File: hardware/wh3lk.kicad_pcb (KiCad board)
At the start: 4 copper layers, 45 x 33.5 mm, 23 parts, among them J1 Eurorack_Power, J2 Conn_01x08_Pin, U1 LD1117S33TR_SOT223, U2 LM4040DBZ-10

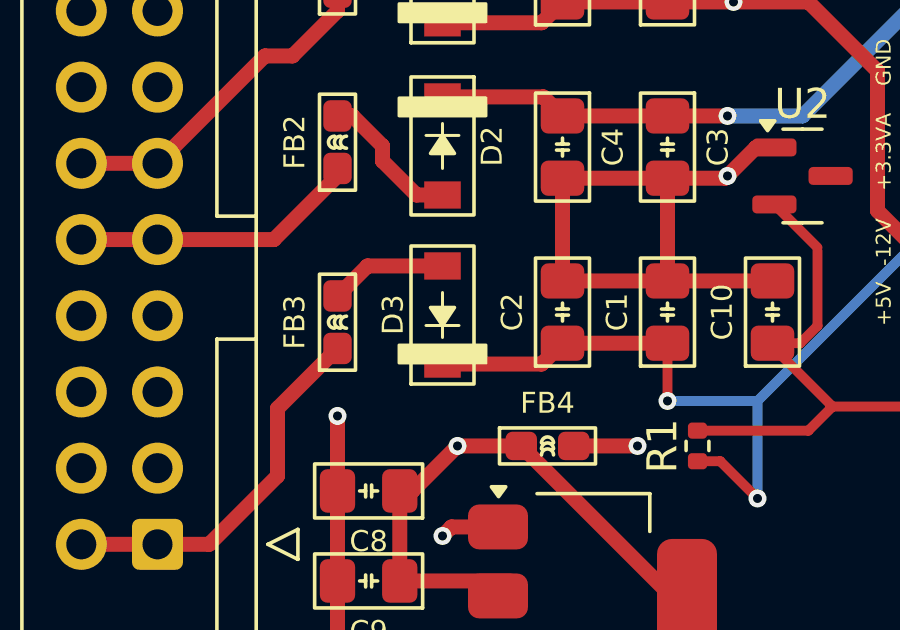
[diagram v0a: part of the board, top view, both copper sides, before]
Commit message: Flipped -12V rail b/c I had it wrong
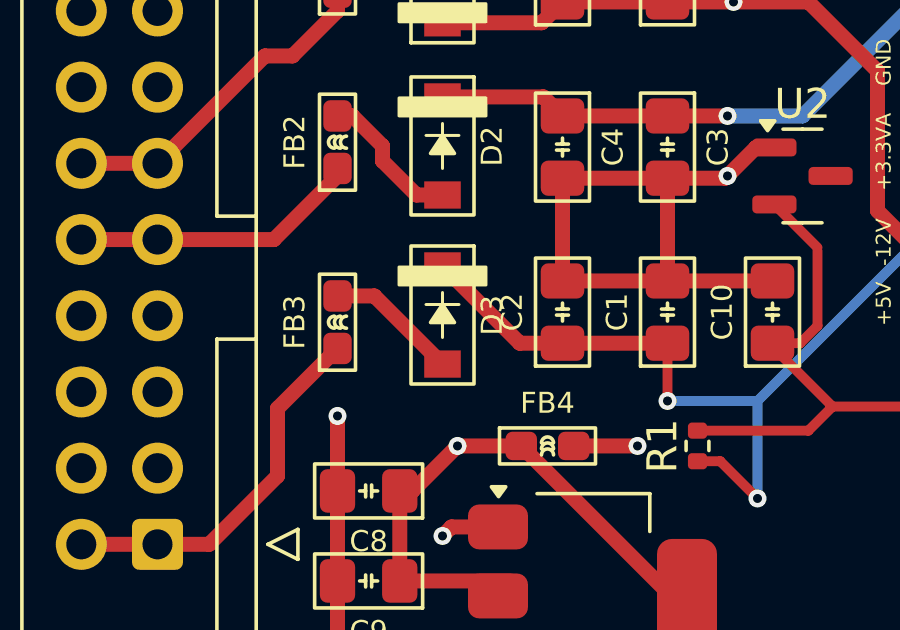
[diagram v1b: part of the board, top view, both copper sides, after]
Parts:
- turned D3 to -90 degrees
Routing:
- net -12V: track 27.9 -> 28.7 mm
- net Net-(D3-A): track 3.91 -> 4.44 mm
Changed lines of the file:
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@@
 	(footprint "winterbloom:D_SOD-123"
 		(layer "F.Cu")
-		(at 73.5 76.635 90)
+		(at 73.5 76.635 -90)
 		(descr "SOD-123")
 		(tags "SOD-123")
 		(property "Reference" "D3"
-			(at 0.01 -1.65 -90)
+			(at 0.01 -1.65 90)
 			(layer "F.SilkS")
 			(effects
@@
 		)
 		(property "Value" "30V"
-			(at 0 2.1 -90)
+			(at 0 2.1 90)
 			(layer "F.Fab")
 			(effects
@@
 		)
 		(property "Footprint" "winterbloom:D_SOD-123"
-			(at 0 0 90)
+			(at 0 0 -90)
 			(unlocked yes)
 			(layer "F.Fab")
@@
 		)
 		(property "Datasheet" ""
-			(at 0 0 90)
+			(at 0 0 -90)
 			(unlocked yes)
 			(layer "F.Fab")
@@
 		)
 		(property "Description" "Diode"
-			(at 0 0 90)
+			(at 0 0 -90)
 			(unlocked yes)
 			(layer "F.Fab")
@@
 		)
 		(property "Sim.Device" "D"
-			(at 0 0 90)
+			(at 0 0 -90)
 			(unlocked yes)
 			(layer "F.Fab")
@@
 		)
 		(property "Sim.Pins" "1=K 2=A"
-			(at 0 0 90)
+			(at 0 0 -90)
 			(unlocked yes)
 			(layer "F.Fab")
@@
 		)
 		(property "LCSC" "C552852"
-			(at 0 0 90)
+			(at 0 0 -90)
 			(unlocked yes)
 			(layer "F.Fab")
@@
 		(attr smd)
 		(fp_line
-			(start 0.25 0)
-			(end 0.75 0)
+			(start -0.75 0)
+			(end -0.35 0)
 			(stroke
 				(width 0.1)
@@
 		(fp_line
 			(start -0.35 0)
-			(end -0.35 -0.55)
+			(end -0.35 0.55)
 			(stroke
 				(width 0.1)
@@
 		(fp_line
 			(start -0.35 0)
-			(end -0.35 0.55)
+			(end -0.35 -0.55)
 			(stroke
 				(width 0.1)
@@
 		)
 		(fp_line
-			(start -0.75 0)
-			(end -0.35 0)
+			(start 0.25 0)
+			(end 0.75 0)
 			(stroke
 				(width 0.1)
@@
 		)
 		(fp_line
-			(start 2 -0.6)
-			(end 2 0.6)
+			(start -0.8 0.6)
+			(end -2 0.6)
 			(stroke
 				(width 0.05)
@@
 		)
 		(fp_line
-			(start 0.8 -0.6)
-			(end 2 -0.6)
+			(start -0.8 0.6)
+			(end -0.8 -0.6)
 			(stroke
 				(width 0.05)
@@
 		)
 		(fp_line
-			(start -0.8 -0.6)
-			(end -2 -0.6)
+			(start 0.8 0.6)
+			(end 2 0.6)
 			(stroke
 				(width 0.05)
@@
 		)
 		(fp_line
-			(start -2 -0.6)
-			(end -2 0.6)
+			(start 0.8 0.6)
+			(end 0.8 -0.6)
 			(stroke
 				(width 0.05)
@@
 		)
 		(fp_line
-			(start 0.8 0.6)
-			(end 0.8 -0.6)
+			(start -2 -0.6)
+			(end -2 0.6)
 			(stroke
 				(width 0.05)
@@
 		)
 		(fp_line
-			(start 0.8 0.6)
-			(end 2 0.6)
+			(start -0.8 -0.6)
+			(end -2 -0.6)
 			(stroke
 				(width 0.05)
@@
 		)
 		(fp_line
-			(start -0.8 0.6)
-			(end -0.8 -0.6)
+			(start 0.8 -0.6)
+			(end 2 -0.6)
 			(stroke
 				(width 0.05)
@@
 		)
 		(fp_line
-			(start -0.8 0.6)
-			(end -2 0.6)
+			(start 2 -0.6)
+			(end 2 0.6)
 			(stroke
 				(width 0.05)
@@
 		)
 		(fp_line
-			(start 2.4 -1.15)
-			(end 2.4 1.15)
+			(start 2.4 1.15)
+			(end -2.4 1.15)
 			(stroke
 				(width 0.05)
@@
 		(fp_line
 			(start -2.4 -1.15)
-			(end 2.4 -1.15)
+			(end -2.4 1.15)
 			(stroke
 				(width 0.05)
@@
 		(fp_line
 			(start -2.4 -1.15)
-			(end -2.4 1.15)
+			(end 2.4 -1.15)
 			(stroke
 				(width 0.05)
@@
 		)
 		(fp_line
-			(start 2.4 1.15)
-			(end -2.4 1.15)
+			(start 2.4 -1.15)
+			(end 2.4 1.15)
 			(stroke
 				(width 0.05)
@@
 		)
 		(fp_line
-			(start 1.6 -1.05)
-			(end 1.6 1.05)
+			(start -1.6 1.05)
+			(end -1.6 -1.05)
 			(stroke
 				(width 0.1)
@@
 		)
 		(fp_line
-			(start -1.6 -1.05)
-			(end 1.6 -1.05)
+			(start 1.6 1.05)
+			(end -1.6 1.05)
 			(stroke
 				(width 0.1)
@@
 		)
 		(fp_line
-			(start 2.3 -0.81)
-			(end 2.3 0.81)
+			(start -1.6 0.81)
+			(end -2.3 0.81)
 			(stroke
 				(width 0.1)
@@
 		)
 		(fp_line
-			(start 1.6 -0.81)
-			(end 2.3 -0.81)
+			(start 1.6 0.81)
+			(end 2.3 0.81)
 			(stroke
 				(width 0.1)
@@
 		)
 		(fp_line
-			(start -1.6 -0.81)
-			(end -2.3 -0.81)
+			(start -2.3 -0.81)
+			(end -2.3 0.81)
 			(stroke
 				(width 0.1)
@@
 		)
 		(fp_line
-			(start -2.3 -0.81)
-			(end -2.3 0.81)
+			(start -1.6 -0.81)
+			(end -2.3 -0.81)
 			(stroke
 				(width 0.1)
@@
 		)
 		(fp_line
-			(start 1.6 0.81)
-			(end 2.3 0.81)
+			(start 1.6 -0.81)
+			(end 2.3 -0.81)
 			(stroke
 				(width 0.1)
@@
 		)
 		(fp_line
-			(start -1.6 0.81)
-			(end -2.3 0.81)
+			(start 2.3 -0.81)
+			(end 2.3 0.81)
 			(stroke
 				(width 0.1)
@@
 		)
 		(fp_line
-			(start 1.6 1.05)
-			(end -1.6 1.05)
+			(start -1.6 -1.05)
+			(end 1.6 -1.05)
 			(stroke
 				(width 0.1)
@@
 		)
 		(fp_line
-			(start -1.6 1.05)
-			(end -1.6 -1.05)
+			(start 1.6 -1.05)
+			(end 1.6 1.05)
 			(stroke
 				(width 0.1)
@@
 		)
 		(fp_text user "${REFERENCE}"
-			(at 0 0 -90)
+			(at 0 0 90)
 			(layer "F.Fab")
 			(effects
@@
 		)
 		(pad "1" smd rect
-			(at -1.635 0 90)
+			(at -1.635 0 270)
 			(size 0.91 1.22)
 			(layers "F.Cu" "F.Paste" "F.Mask")
@@
 		)
 		(pad "2" smd rect
-			(at 1.635 0 90)
+			(at 1.635 0 270)
 			(size 0.91 1.22)
 			(layers "F.Cu" "F.Paste" "F.Mask")
@@
 	)
 	(segment
-		(start 73.5 78.27)
-		(end 76.805 78.27)
+		(start 76.075 77.575)
+		(end 77.5 77.575)
 		(width 0.5)
 		(layer "F.Cu")
@@
 	)
 	(segment
-		(start 76.805 78.27)
-		(end 77.5 77.575)
+		(start 73.5 75)
+		(end 76.075 77.575)
 		(width 0.5)
 		(layer "F.Cu")
@@
 	)
 	(segment
-		(start 71 75)
-		(end 70 76)
+		(start 71.23 76)
+		(end 73.5 78.27)
 		(width 0.5)
 		(layer "F.Cu")
@@
 	)
 	(segment
-		(start 73.5 75)
-		(end 71 75)
+		(start 70 76)
+		(end 71.23 76)
 		(width 0.5)
 		(layer "F.Cu")

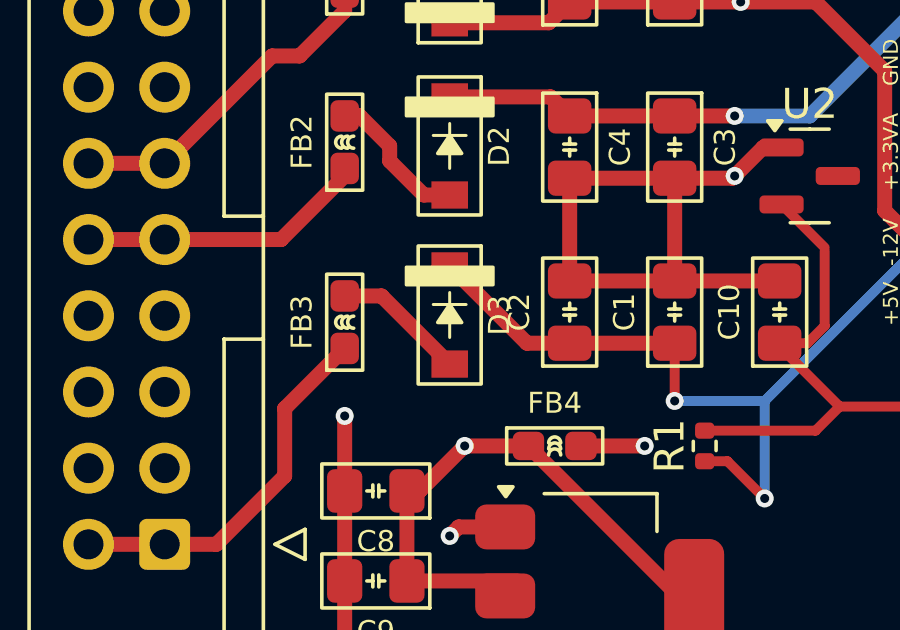
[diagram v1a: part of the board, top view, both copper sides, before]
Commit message: ok, REALLY fixed the -12v diode
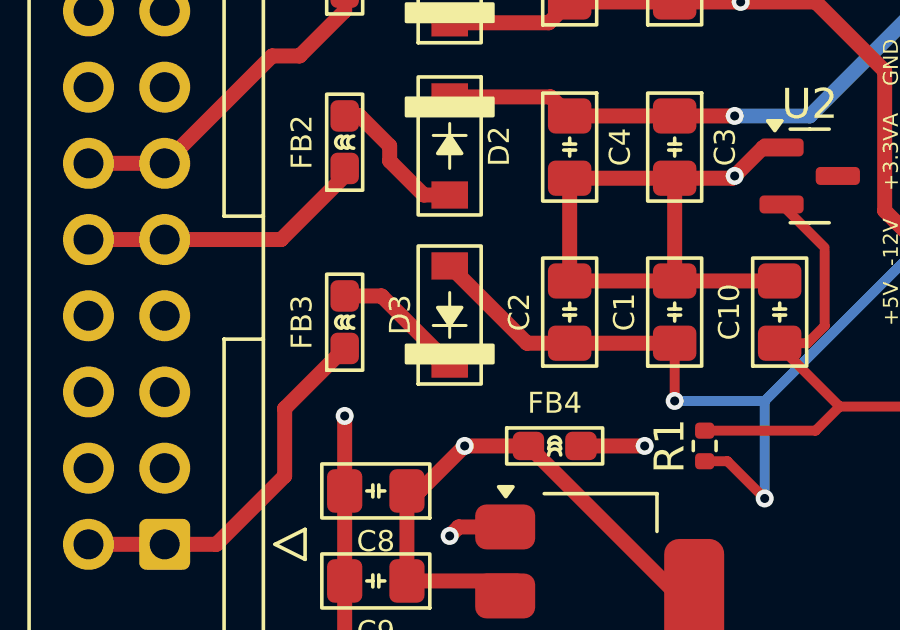
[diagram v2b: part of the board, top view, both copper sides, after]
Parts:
- turned D3 to 90 degrees
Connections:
- D3 pad 1: -12V -> Net-(D3-K)
- D3 pad 2: Net-(D3-A) -> -12V
- FB3 pad 2: Net-(D3-A) -> Net-(D3-K)
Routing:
- net Net-(D3-K): track 0.00 -> 4.44 mm
- net Net-(D3-A): track 4.44 -> 0.00 mm
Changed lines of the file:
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@@
 	(net 7 "Net-(D1-A)")
 	(net 8 "Net-(D2-A)")
-	(net 9 "Net-(D3-A)")
+	(net 9 "Net-(D3-K)")
 	(net 10 "RACK+5V")
 	(net 11 "RACK+12V")
@@
 	(footprint "winterbloom:D_SOD-123"
 		(layer "F.Cu")
-		(at 73.5 76.635 -90)
+		(at 73.5 76.635 90)
 		(descr "SOD-123")
 		(tags "SOD-123")
 		(property "Reference" "D3"
-			(at 0.01 -1.65 90)
+			(at 0.01 -1.65 270)
 			(layer "F.SilkS")
 			(effects
@@
 		)
 		(property "Value" "30V"
-			(at 0 2.1 90)
+			(at 0 2.1 270)
 			(layer "F.Fab")
 			(effects
@@
 		)
 		(property "Footprint" "winterbloom:D_SOD-123"
-			(at 0 0 -90)
+			(at 0 0 90)
 			(unlocked yes)
 			(layer "F.Fab")
@@
 		)
 		(property "Datasheet" ""
-			(at 0 0 -90)
+			(at 0 0 90)
 			(unlocked yes)
 			(layer "F.Fab")
@@
 		)
 		(property "Description" "Diode"
-			(at 0 0 -90)
+			(at 0 0 90)
 			(unlocked yes)
 			(layer "F.Fab")
@@
 		)
 		(property "Sim.Device" "D"
-			(at 0 0 -90)
+			(at 0 0 90)
 			(unlocked yes)
 			(layer "F.Fab")
@@
 		)
 		(property "Sim.Pins" "1=K 2=A"
-			(at 0 0 -90)
+			(at 0 0 90)
 			(unlocked yes)
 			(layer "F.Fab")
@@
 		)
 		(property "LCSC" "C552852"
-			(at 0 0 -90)
+			(at 0 0 90)
 			(unlocked yes)
 			(layer "F.Fab")
@@
 		(attr smd)
 		(fp_line
-			(start -0.75 0)
-			(end -0.35 0)
+			(start 0.25 0)
+			(end 0.75 0)
 			(stroke
 				(width 0.1)
@@
 		(fp_line
 			(start -0.35 0)
-			(end -0.35 0.55)
+			(end -0.35 -0.55)
 			(stroke
 				(width 0.1)
@@
 		(fp_line
 			(start -0.35 0)
-			(end -0.35 -0.55)
+			(end -0.35 0.55)
 			(stroke
 				(width 0.1)
@@
 		)
 		(fp_line
-			(start 0.25 0)
-			(end 0.75 0)
+			(start -0.75 0)
+			(end -0.35 0)
 			(stroke
 				(width 0.1)
@@
 		)
 		(fp_line
-			(start -0.8 0.6)
-			(end -2 0.6)
+			(start 2 -0.6)
+			(end 2 0.6)
 			(stroke
 				(width 0.05)
@@
 		)
 		(fp_line
-			(start -0.8 0.6)
-			(end -0.8 -0.6)
+			(start 0.8 -0.6)
+			(end 2 -0.6)
 			(stroke
 				(width 0.05)
@@
 		)
 		(fp_line
-			(start 0.8 0.6)
-			(end 2 0.6)
+			(start -0.8 -0.6)
+			(end -2 -0.6)
 			(stroke
 				(width 0.05)
@@
 		)
 		(fp_line
-			(start 0.8 0.6)
-			(end 0.8 -0.6)
+			(start -2 -0.6)
+			(end -2 0.6)
 			(stroke
 				(width 0.05)
@@
 		)
 		(fp_line
-			(start -2 -0.6)
-			(end -2 0.6)
+			(start 0.8 0.6)
+			(end 0.8 -0.6)
 			(stroke
 				(width 0.05)
@@
 		)
 		(fp_line
-			(start -0.8 -0.6)
-			(end -2 -0.6)
+			(start 0.8 0.6)
+			(end 2 0.6)
 			(stroke
 				(width 0.05)
@@
 		)
 		(fp_line
-			(start 0.8 -0.6)
-			(end 2 -0.6)
+			(start -0.8 0.6)
+			(end -0.8 -0.6)
 			(stroke
 				(width 0.05)
@@
 		)
 		(fp_line
-			(start 2 -0.6)
-			(end 2 0.6)
+			(start -0.8 0.6)
+			(end -2 0.6)
 			(stroke
 				(width 0.05)
@@
 		)
 		(fp_line
-			(start 2.4 1.15)
-			(end -2.4 1.15)
+			(start 2.4 -1.15)
+			(end 2.4 1.15)
 			(stroke
 				(width 0.05)
@@
 		(fp_line
 			(start -2.4 -1.15)
-			(end -2.4 1.15)
+			(end 2.4 -1.15)
 			(stroke
 				(width 0.05)
@@
 		(fp_line
 			(start -2.4 -1.15)
-			(end 2.4 -1.15)
+			(end -2.4 1.15)
 			(stroke
 				(width 0.05)
@@
 		)
 		(fp_line
-			(start 2.4 -1.15)
-			(end 2.4 1.15)
+			(start 2.4 1.15)
+			(end -2.4 1.15)
 			(stroke
 				(width 0.05)
@@
 		)
 		(fp_line
-			(start -1.6 1.05)
-			(end -1.6 -1.05)
+			(start 1.6 -1.05)
+			(end 1.6 1.05)
 			(stroke
 				(width 0.1)
@@
 		)
 		(fp_line
-			(start 1.6 1.05)
-			(end -1.6 1.05)
+			(start -1.6 -1.05)
+			(end 1.6 -1.05)
 			(stroke
 				(width 0.1)
@@
 		)
 		(fp_line
-			(start -1.6 0.81)
-			(end -2.3 0.81)
+			(start 2.3 -0.81)
+			(end 2.3 0.81)
 			(stroke
 				(width 0.1)
@@
 		)
 		(fp_line
-			(start 1.6 0.81)
-			(end 2.3 0.81)
+			(start 1.6 -0.81)
+			(end 2.3 -0.81)
 			(stroke
 				(width 0.1)
@@
 		)
 		(fp_line
-			(start -2.3 -0.81)
-			(end -2.3 0.81)
+			(start -1.6 -0.81)
+			(end -2.3 -0.81)
 			(stroke
 				(width 0.1)
@@
 		)
 		(fp_line
-			(start -1.6 -0.81)
-			(end -2.3 -0.81)
+			(start -2.3 -0.81)
+			(end -2.3 0.81)
 			(stroke
 				(width 0.1)
@@
 		)
 		(fp_line
-			(start 1.6 -0.81)
-			(end 2.3 -0.81)
+			(start 1.6 0.81)
+			(end 2.3 0.81)
 			(stroke
 				(width 0.1)
@@
 		)
 		(fp_line
-			(start 2.3 -0.81)
-			(end 2.3 0.81)
+			(start -1.6 0.81)
+			(end -2.3 0.81)
 			(stroke
 				(width 0.1)
@@
 		)
 		(fp_line
-			(start -1.6 -1.05)
-			(end 1.6 -1.05)
+			(start 1.6 1.05)
+			(end -1.6 1.05)
 			(stroke
 				(width 0.1)
@@
 		)
 		(fp_line
-			(start 1.6 -1.05)
-			(end 1.6 1.05)
+			(start -1.6 1.05)
+			(end -1.6 -1.05)
 			(stroke
 				(width 0.1)
@@
 		)
 		(fp_text user "${REFERENCE}"
-			(at 0 0 90)
+			(at 0 0 270)
 			(layer "F.Fab")
 			(effects
@@
 		)
 		(pad "1" smd rect
-			(at -1.635 0 270)
+			(at -1.635 0 90)
 			(size 0.91 1.22)
 			(layers "F.Cu" "F.Paste" "F.Mask")
-			(net 2 "-12V")
+			(net 9 "Net-(D3-K)")
 			(pinfunction "K")
 			(pintype "passive")
 		)
 		(pad "2" smd rect
-			(at 1.635 0 270)
+			(at 1.635 0 90)
 			(size 0.91 1.22)
 			(layers "F.Cu" "F.Paste" "F.Mask")
-			(net 9 "Net-(D3-A)")
+			(net 2 "-12V")
 			(pinfunction "A")
 			(pintype "passive")
@@
 			)
 		)
-		(property "LCSC" "C7411876"
+		(property "LCSC" "C77456"
 			(at 0 0 180)
 			(unlocked yes)
@@
 			)
 		)
-		(property "LCSC" "C3717582"
+		(property "LCSC" "C201738"
 			(at 0 0 0)
 			(unlocked yes)
@@
 			)
 		)
-		(property "LCSC" "C17314042"
+		(property "LCSC" "C17024"
 			(at 0 0 180)
 			(unlocked yes)
@@
 			)
 		)
-		(property "LCSC" "C6549338"
+		(property "LCSC" "C284423"
 			(at 0 0 90)
 			(unlocked yes)
@@
 			(layers "F.Cu" "F.Paste" "F.Mask")
 			(roundrect_rratio 0.25)
-			(net 9 "Net-(D3-A)")
+			(net 9 "Net-(D3-K)")
 			(pintype "passive")
 		)
